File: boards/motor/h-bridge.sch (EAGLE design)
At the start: 11 parts

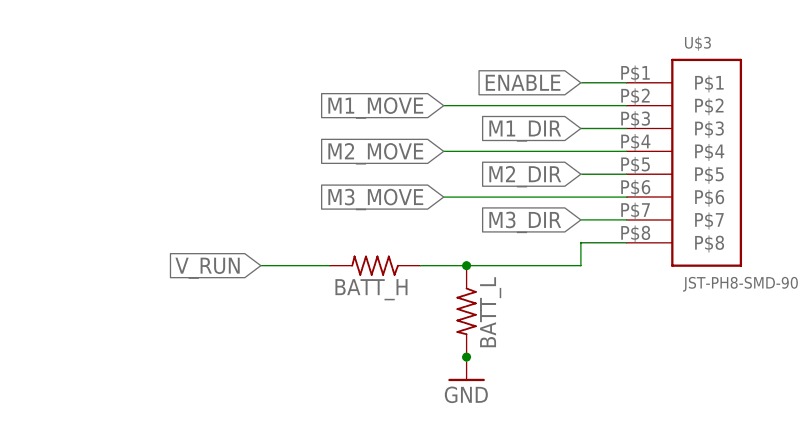
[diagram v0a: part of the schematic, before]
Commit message: text change for V_batt resistors
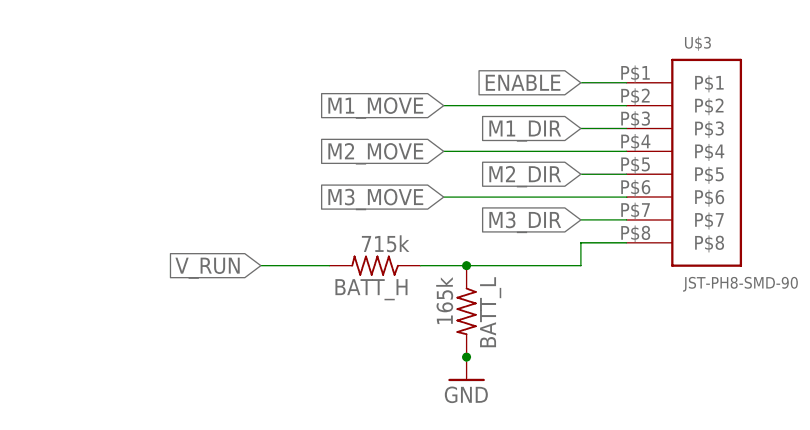
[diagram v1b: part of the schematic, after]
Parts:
- BATT_H: value (none) -> 715k
- BATT_L: value (none) -> 165k
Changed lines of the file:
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@@
 <part name="U$1" library="wolfbot" deviceset="ESWITCH-WSP1" device=""/>
 <part name="R1" library="resistor" deviceset="R-US_" device="R0603"/>
-<part name="BATT_H" library="resistor" deviceset="R-US_" device="R0603"/>
-<part name="BATT_L" library="resistor" deviceset="R-US_" device="R0603"/>
+<part name="BATT_H" library="resistor" deviceset="R-US_" device="R0603" value="715k"/>
+<part name="BATT_L" library="resistor" deviceset="R-US_" device="R0603" value="165k"/>
 <part name="GND7" library="supply1" deviceset="GND" device=""/>
 <part name="U$3" library="jst-ph" deviceset="JST-PH8-SMD-90*" device=""/>

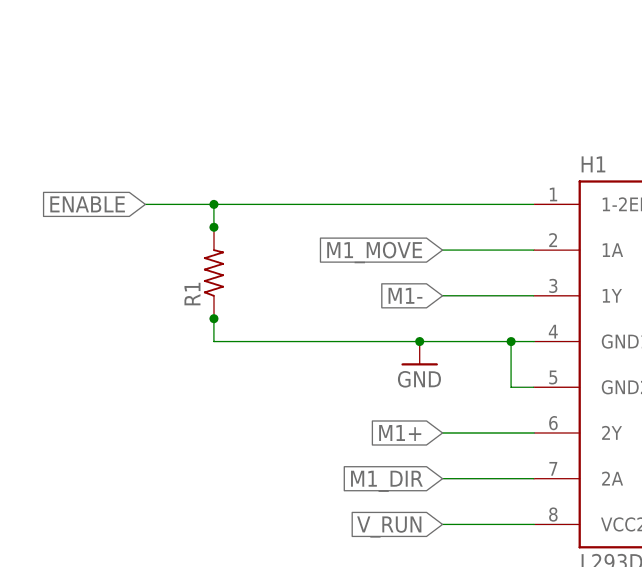
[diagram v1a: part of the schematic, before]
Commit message: Fix motor board silk screening
- add tValues and bValues to CAM job
- move resistor labels
- remove unwanted labels
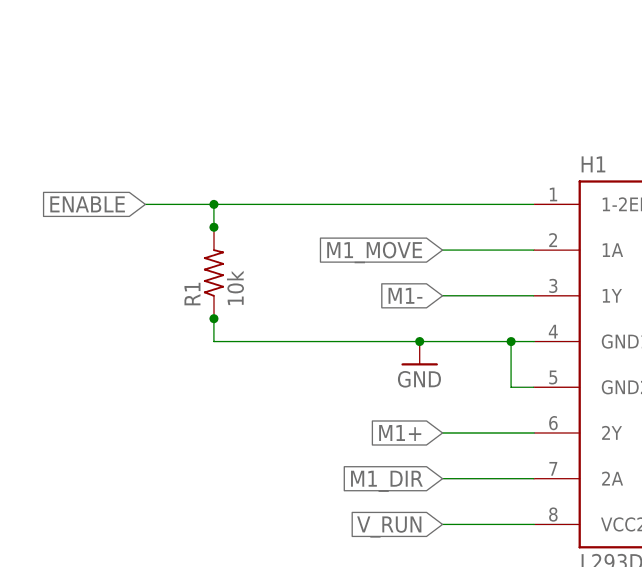
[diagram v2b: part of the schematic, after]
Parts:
- R1: value (none) -> 10k
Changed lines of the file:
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@@
 <part name="GND6" library="supply1" deviceset="GND" device=""/>
 <part name="U$1" library="wolfbot" deviceset="ESWITCH-WSP1" device=""/>
-<part name="R1" library="resistor" deviceset="R-US_" device="R0603"/>
+<part name="R1" library="resistor" deviceset="R-US_" device="R0603" value="10k"/>
 <part name="BATT_H" library="resistor" deviceset="R-US_" device="R0603" value="715k"/>
 <part name="BATT_L" library="resistor" deviceset="R-US_" device="R0603" value="165k"/>

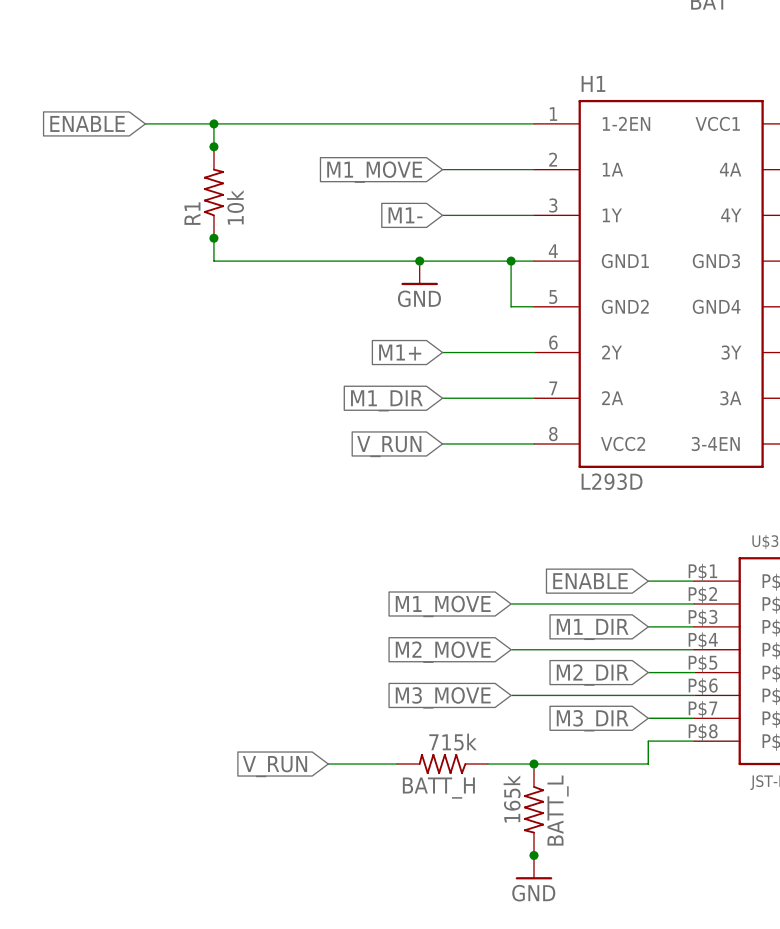
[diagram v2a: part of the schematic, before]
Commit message: Fixed pull down, and three res sizes
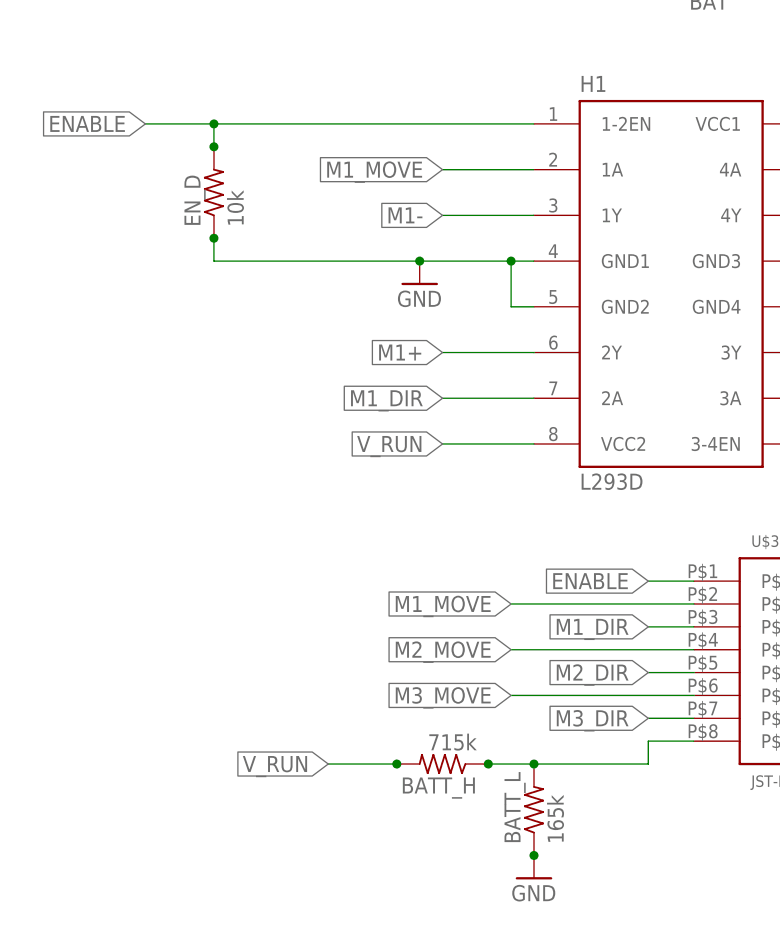
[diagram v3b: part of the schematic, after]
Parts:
- removed R1: 10k, resistor:R-US_R0603
- added EN_D: 10k, resistor:R-US_R0805
- BATT_H, BATT_L: device resistor:R-US_R0603 -> resistor:R-US_R0805
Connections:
- net ENABLE: now also EN_D.2; no longer R1.2
- net GND: now also BATT_L.1, EN_D.1; no longer BATT_L.2, R1.1
- net N$2: now also BATT_L.2; no longer BATT_L.1
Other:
- moved on the sheet: BATT_L
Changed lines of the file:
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@@
 <?xml version="1.0" encoding="utf-8"?>
 <!DOCTYPE eagle SYSTEM "eagle.dtd">
-<eagle version="6.4">
+<eagle version="6.5.0">
 <drawing>
 <settings>
@@
 <part name="GND6" library="supply1" deviceset="GND" device=""/>
 <part name="U$1" library="wolfbot" deviceset="ESWITCH-WSP1" device=""/>
-<part name="R1" library="resistor" deviceset="R-US_" device="R0603" value="10k"/>
-<part name="BATT_H" library="resistor" deviceset="R-US_" device="R0603" value="715k"/>
-<part name="BATT_L" library="resistor" deviceset="R-US_" device="R0603" value="165k"/>
 <part name="GND7" library="supply1" deviceset="GND" device=""/>
 <part name="U$3" library="jst-ph" deviceset="JST-PH8-SMD-90*" device=""/>
+<part name="EN_D" library="resistor" deviceset="R-US_" device="R0805" value="10k"/>
+<part name="BATT_L" library="resistor" deviceset="R-US_" device="R0805" value="165k"/>
+<part name="BATT_H" library="resistor" deviceset="R-US_" device="R0805" value="715k"/>
 </parts>
 <sheets>
@@
 <instance part="GND6" gate="1" x="109.22" y="119.38"/>
 <instance part="U$1" gate="G$1" x="83.82" y="111.76"/>
-<instance part="R1" gate="G$1" x="-2.54" y="81.28" rot="R90"/>
-<instance part="BATT_H" gate="G$1" x="22.86" y="17.78" rot="R180"/>
-<instance part="BATT_L" gate="G$1" x="33.02" y="12.7" rot="R270"/>
 <instance part="GND7" gate="1" x="33.02" y="5.08"/>
 <instance part="U$3" gate="G$1" x="60.96" y="30.48"/>
+<instance part="EN_D" gate="G$1" x="-2.54" y="81.28" rot="R90"/>
+<instance part="BATT_L" gate="G$1" x="33.02" y="12.7" rot="R90"/>
+<instance part="BATT_H" gate="G$1" x="22.86" y="17.78" rot="R180"/>
 </instances>
 <busses>
@@
 <pinref part="H1" gate="G$1" pin="GND2"/>
 <wire x1="33.02" y1="68.58" x2="30.48" y2="68.58" width="0.1524" layer="91"/>
-<pinref part="R1" gate="G$1" pin="1"/>
 <wire x1="-2.54" y1="76.2" x2="-2.54" y2="73.66" width="0.1524" layer="91"/>
 <wire x1="-2.54" y1="73.66" x2="20.32" y2="73.66" width="0.1524" layer="91"/>
+<junction x="20.32" y="73.66"/>
+<pinref part="EN_D" gate="G$1" pin="1"/>
 <junction x="-2.54" y="76.2"/>
-<junction x="20.32" y="73.66"/>
 </segment>
 <segment>
@@
 </segment>
 <segment>
-<pinref part="BATT_L" gate="G$1" pin="2"/>
 <pinref part="GND7" gate="1" pin="GND"/>
+<pinref part="BATT_L" gate="G$1" pin="1"/>
 <junction x="33.02" y="7.62"/>
 </segment>
@@
 <wire x1="-2.54" y1="88.9" x2="-10.16" y2="88.9" width="0.1524" layer="91"/>
 <wire x1="-2.54" y1="88.9" x2="-2.54" y2="86.36" width="0.1524" layer="91"/>
-<pinref part="R1" gate="G$1" pin="2"/>
+<junction x="-2.54" y="88.9"/>
+<pinref part="EN_D" gate="G$1" pin="2"/>
 <junction x="-2.54" y="86.36"/>
-<junction x="-2.54" y="88.9"/>
 </segment>
 <segment>
@@
 <segment>
 <label x="10.16" y="17.78" size="1.778" layer="95" rot="R180" xref="yes"/>
+<wire x1="10.16" y1="17.78" x2="17.78" y2="17.78" width="0.1524" layer="91"/>
 <pinref part="BATT_H" gate="G$1" pin="2"/>
-<wire x1="10.16" y1="17.78" x2="17.78" y2="17.78" width="0.1524" layer="91"/>
+<junction x="17.78" y="17.78"/>
 </segment>
 <segment>
@@
 <net name="N$2" class="0">
 <segment>
-<pinref part="BATT_H" gate="G$1" pin="1"/>
 <wire x1="27.94" y1="17.78" x2="33.02" y2="17.78" width="0.1524" layer="91"/>
 <wire x1="33.02" y1="17.78" x2="45.72" y2="17.78" width="0.1524" layer="91"/>
 <wire x1="45.72" y1="17.78" x2="45.72" y2="20.32" width="0.1524" layer="91"/>
 <wire x1="45.72" y1="20.32" x2="50.8" y2="20.32" width="0.1524" layer="91"/>
-<pinref part="BATT_L" gate="G$1" pin="1"/>
+<pinref part="U$3" gate="G$1" pin="P$8"/>
+<pinref part="BATT_H" gate="G$1" pin="1"/>
+<pinref part="BATT_L" gate="G$1" pin="2"/>
 <junction x="33.02" y="17.78"/>
-<pinref part="U$3" gate="G$1" pin="P$8"/>
-</segment>
-</net>
+<junction x="27.94" y="17.78"/>
+</segment>
+</net>
